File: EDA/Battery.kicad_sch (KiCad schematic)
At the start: 0 parts

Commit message: Changed PD IC from TPS25750DRJKR to TPS25730DREFR
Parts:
- added J1: 12402012E212A, CANSAT-lib:AMPHENOL_USB-C_12402012E212A, symbol CANSAT-lib:12402012E212A
- added U10: TPS25730DREFR, CANSAT-lib:REF0038A-MFG, symbol CANSAT-lib:TPS25730DREFR
- added U9: BQ25895RTWT, CANSAT-lib:QFN50P400X400X80-25N, symbol CANSAT-lib:BQ25895RTWT
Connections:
- new net: U10.11 (GND), U10.12 (GND), U10.14 (GND), U10.16 (GND), U10.17 (GND), U10.31 (GND), U10.34 (GND), U10.35 (GND)
- new net CC1_A: J1.A5 (CC1_A), U10.28 (CC1)
- new net CC1_B: J1.B5 (CC1_B), U10.29 (CC2)
- new net D+: J1.A6 (D+_A), J1.B6 (D+_B)
- new net D-: J1.A7 (D-_A), J1.B7 (D-_B)
- new net GND: J1.A1_B12 (GND), J1.B1_A12 (GND__1), J1.SH1 (SHIELD), J1.SH2 (SHIELD__1), J1.SH3 (SHIELD__2), J1.SH4 (SHIELD__3)
- new net VBUS: J1.A4_B9 (VBUS), J1.B4_A9 (VBUS__1), U10.23 (VBUS_IN), U10.24 (VBUS_IN), U10.25 (VBUS_IN)
- no-connect marks 0 -> 6

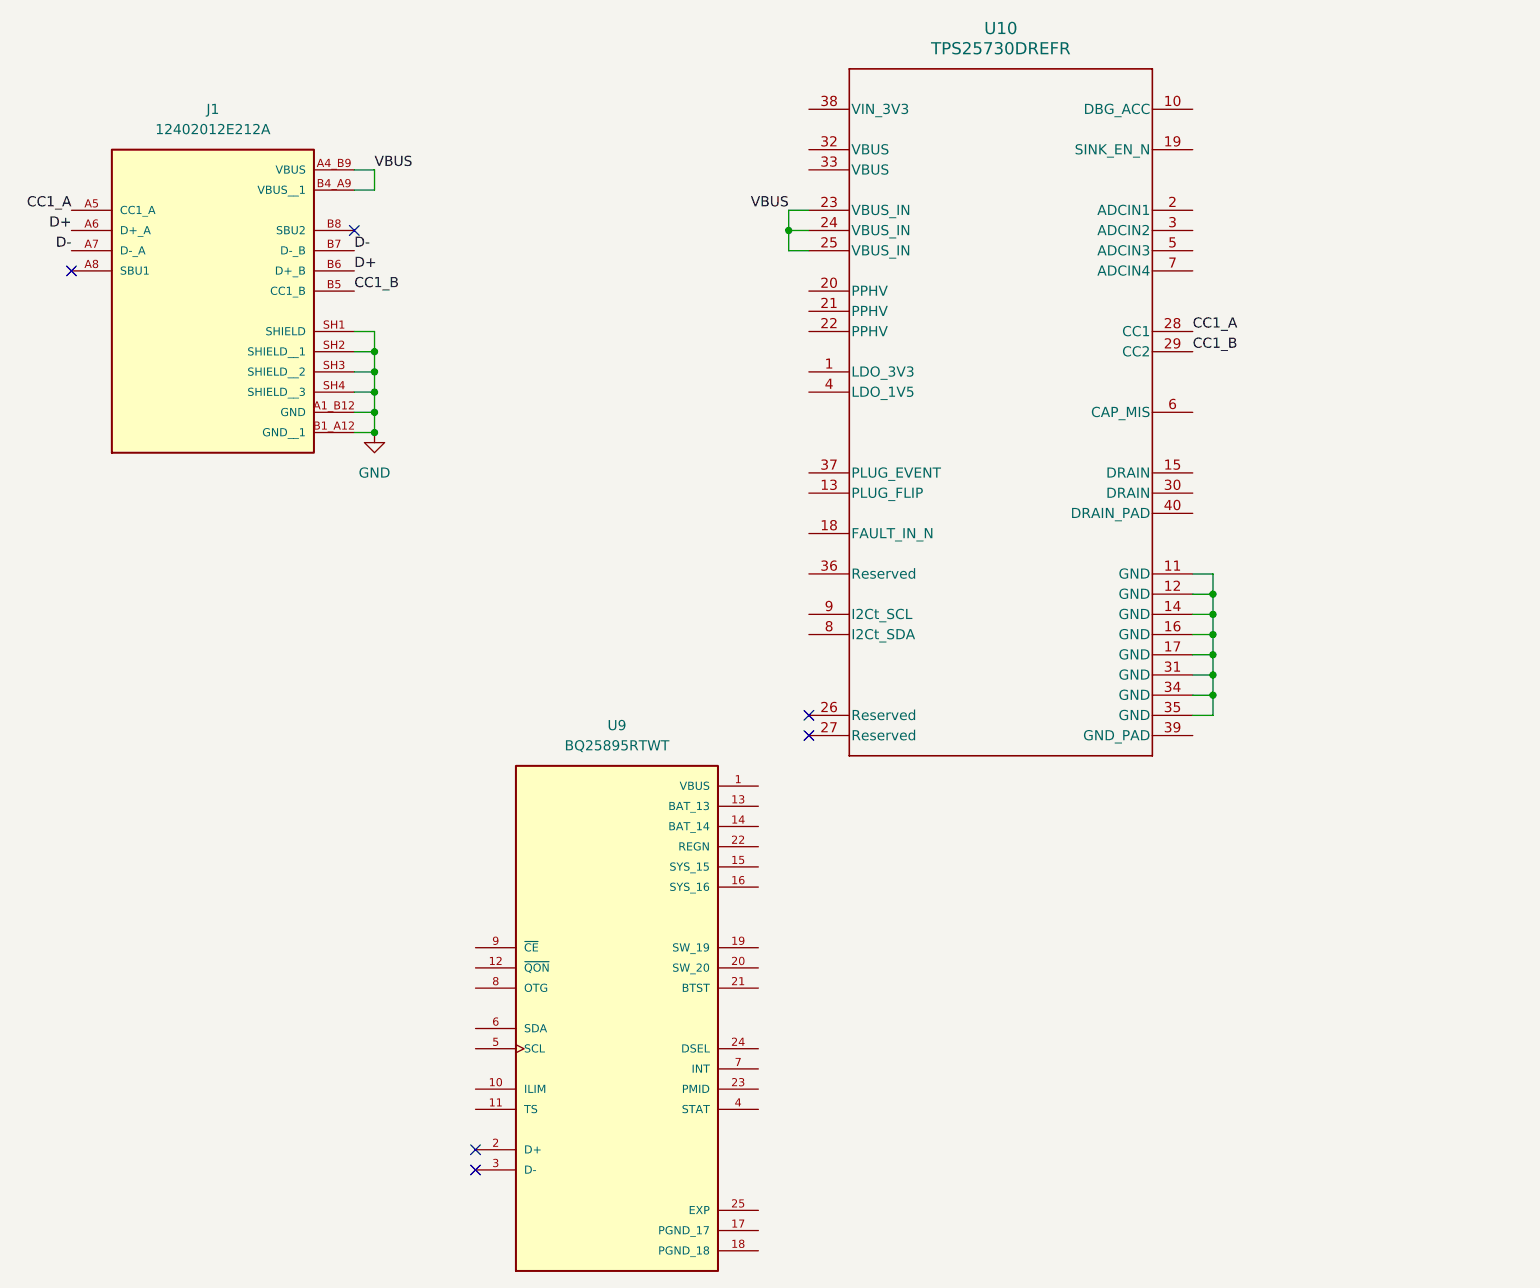
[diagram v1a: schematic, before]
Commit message: added smoothing capacitors to PD IC
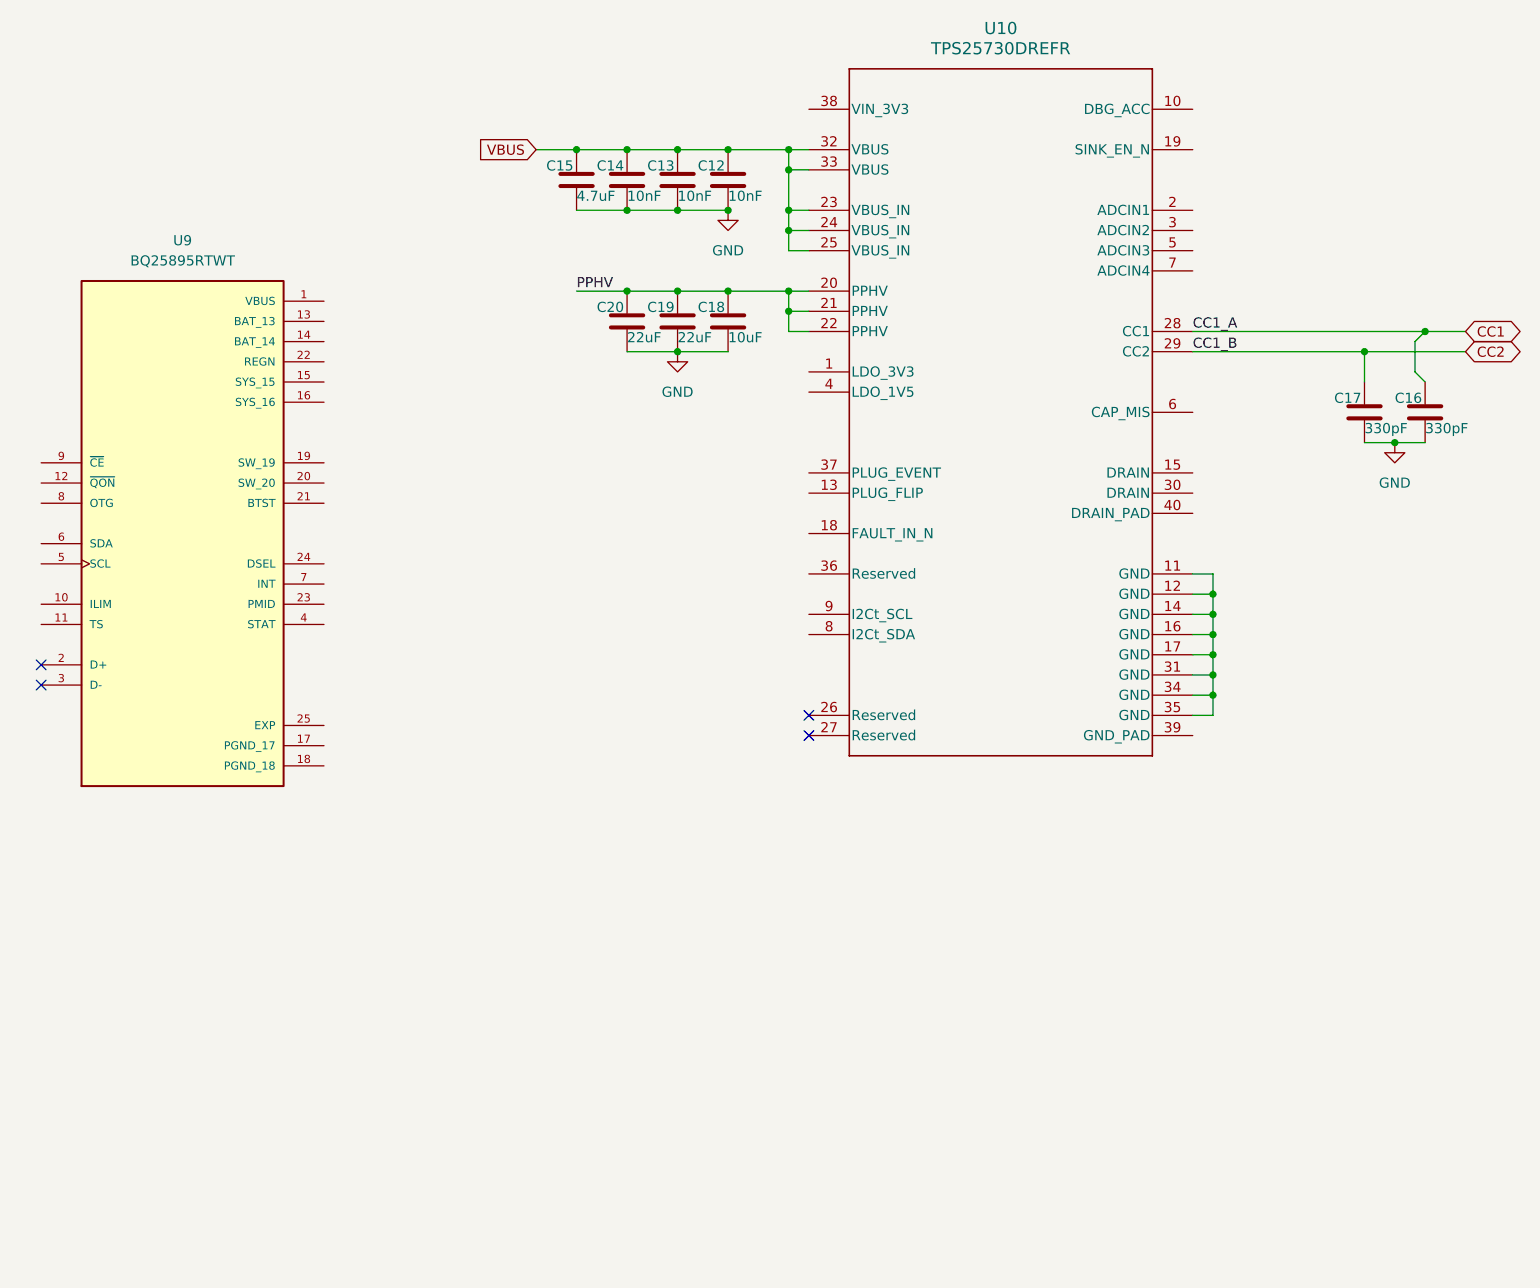
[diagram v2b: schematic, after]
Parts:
- removed J1: 12402012E212A, CANSAT-lib:AMPHENOL_USB-C_12402012E212A, symbol CANSAT-lib:12402012E212A
- added C12, C13, C14: 10nF, symbol Device:C
- added C15: 4.7uF, symbol Device:C
- added C16, C17: 330pF, symbol Device:C
- added C18: 10uF, symbol Device:C
- added C19, C20: 22uF, symbol Device:C
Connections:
- net GND: now also C12.2, C13.2, C14.2, C15.2, C16.2, C17.2, C18.2, C19.2, C20.2
- net VBUS: now also U10.32 (VBUS), U10.33 (VBUS), C12.1, C13.1, C14.1, C15.1
- net PPHV: now reaches U10.20 (PPHV)
- net PPHV: now also U10.21 (PPHV), U10.22 (PPHV), C18.1, C19.1, C20.1
- net CC1_A renamed CC1
- net CC1: now also C16.1
- net CC1_B renamed CC2
- net CC2: now also C17.1
- no-connect marks 6 -> 4
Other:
- moved on the sheet: U9

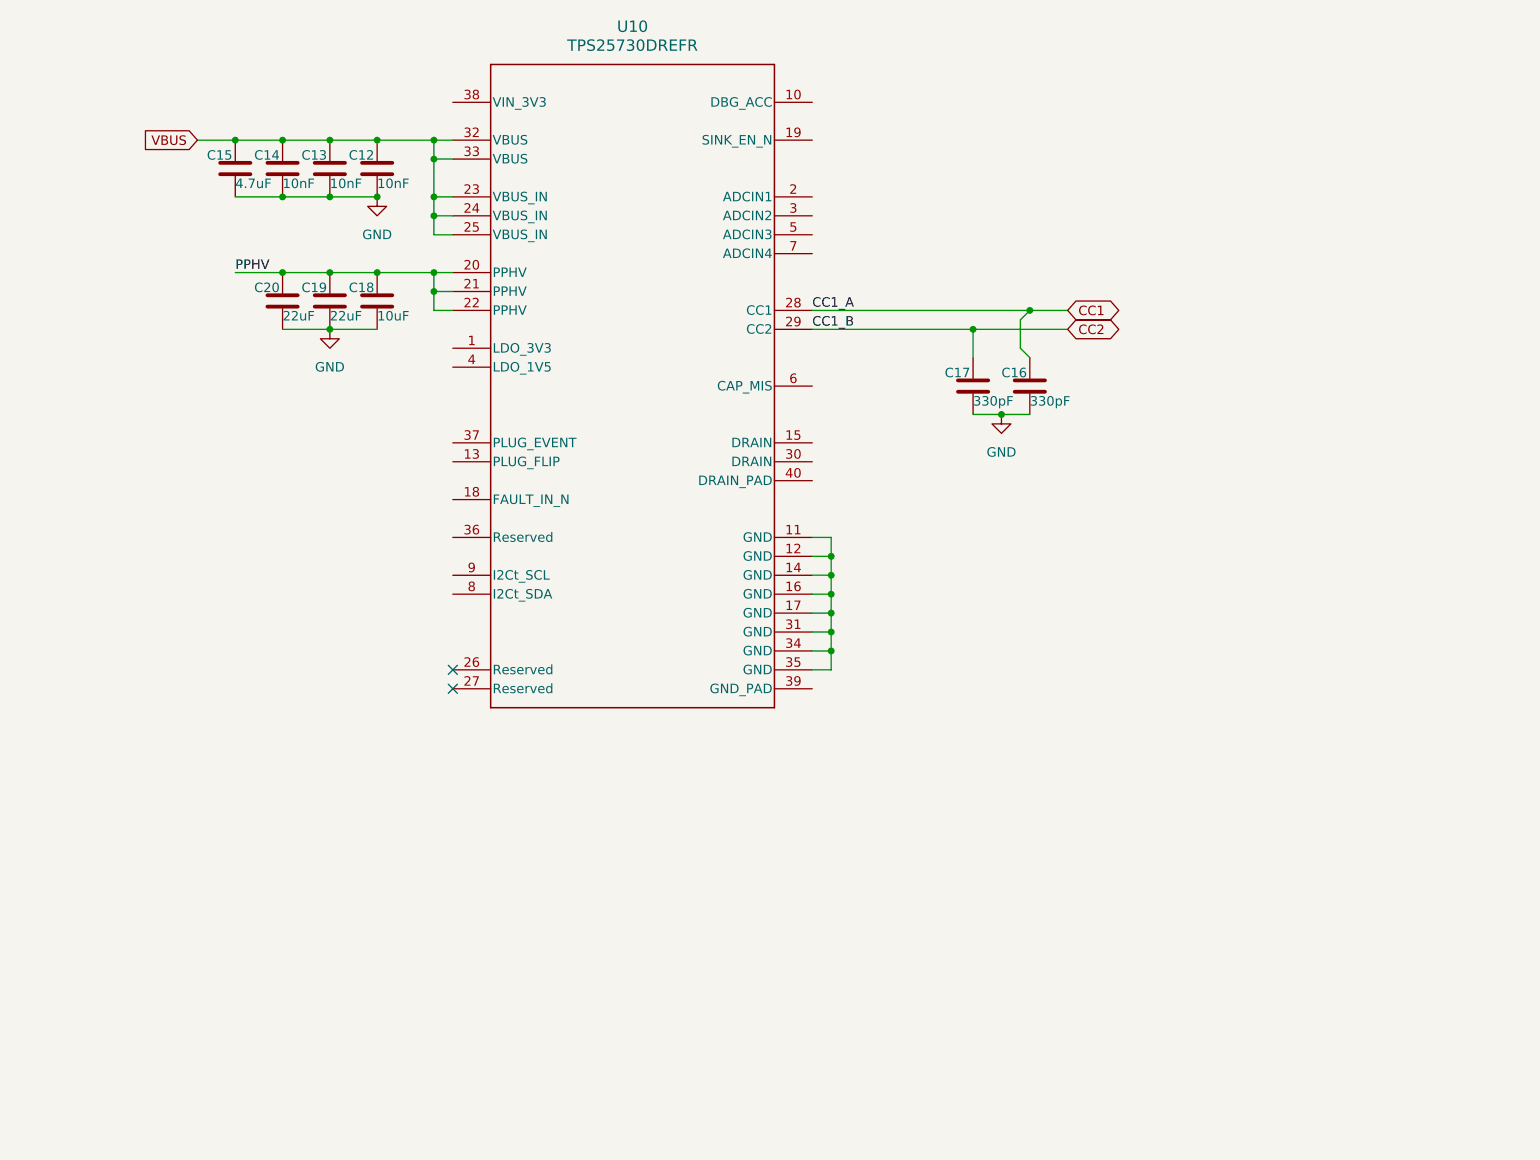
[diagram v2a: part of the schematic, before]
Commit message: PD negotiator IC wired up in schematic
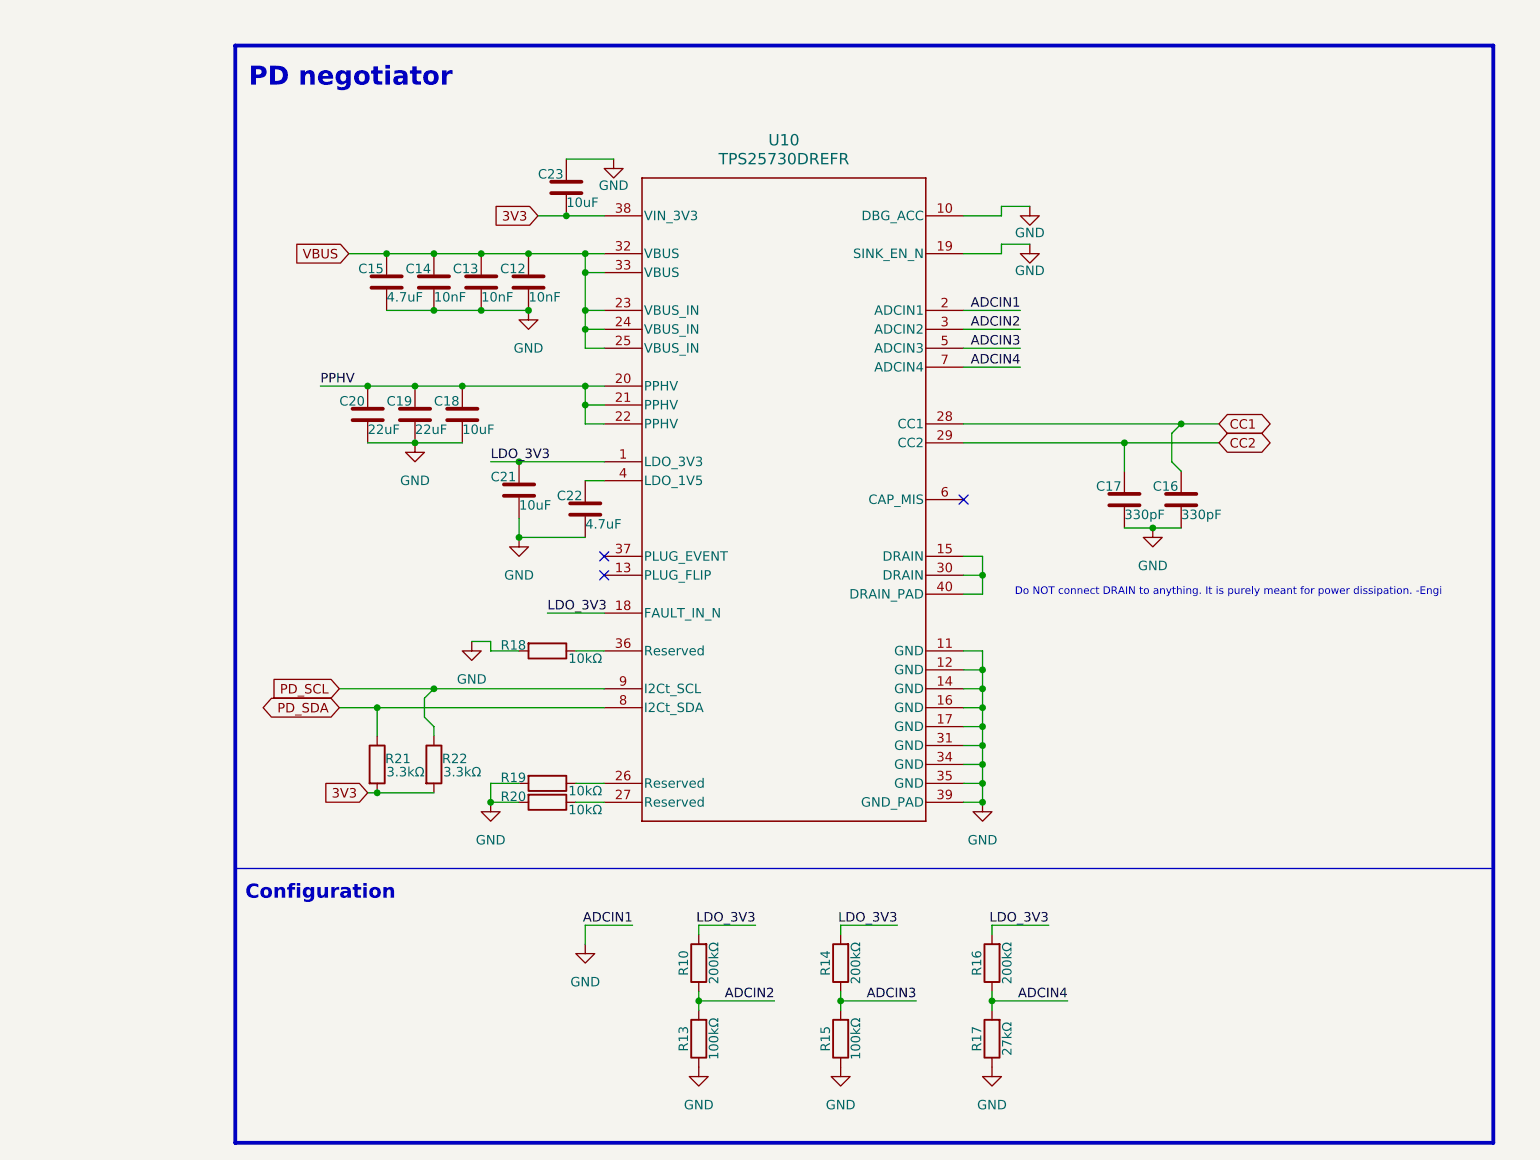
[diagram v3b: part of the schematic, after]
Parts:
- added C21, C23: 10uF, symbol Device:C
- added C22: 4.7uF, symbol Device:C
- added R10, R14, R16: 200kΩ, symbol Device:R
- added R13, R15: 100kΩ, symbol Device:R
- added R17: 27kΩ, symbol Device:R
- added R18, R19, R20: 10kΩ, symbol Device:R
- added R21, R22: 3.3kΩ, symbol Device:R
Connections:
- net GND: now also U10.10 (DBG_ACC), U10.11 (GND), U10.12 (GND), U10.14 (GND), U10.16 (GND), U10.17 (GND), U10.19 (SINK_EN_N), U10.2 (ADCIN1), U10.31 (GND), U10.34 (GND), U10.35 (GND), U10.39 (GND_PAD), C21.2, C22.2, C23.1, R13.1, R15.1, R17.1, R18.2, R19.2, R20.2
- net LDO_3V3: now reaches U10.1 (LDO_3V3)
- net LDO_3V3: now also U10.18 (FAULT_IN_N), C21.1, R10.2, R14.2, R16.2
- net at U10.15 (DRAIN): now also U10.30 (DRAIN), U10.40 (DRAIN_PAD)
- net at U10.26 (Reserved): now also R19.1
- net at U10.27 (Reserved): now also R20.1
- net ADCIN2: now reaches U10.3 (ADCIN2)
- net ADCIN2: now also R10.1, R13.2
- net at U10.36 (Reserved): now also R18.1
- net 3V3: now reaches U10.38 (VIN_3V3)
- net 3V3: now also C23.2, R21.2, R22.2
- net at U10.4 (LDO_1V5): now also C22.1
- net ADCIN3: now reaches U10.5 (ADCIN3)
- net ADCIN3: now also R14.1, R15.2
- net ADCIN4: now reaches U10.7 (ADCIN4)
- net ADCIN4: now also R16.1, R17.2
- net PD_SDA: now reaches U10.8 (I2Ct_SDA)
- net PD_SDA: now also R21.1
- net PD_SCL: now reaches U10.9 (I2Ct_SCL)
- net PD_SCL: now also R22.1
- no-connect marks 4 -> 5
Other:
- note added: "Configuration"
- note added: "Do NOT connect DRAIN to anything. It is purely meant for power dissipation. -Engi"
- note added: "PD negotiator"
- moved on the sheet: C12, C13, C14, C15, C16, C17, C18, C19, C20, U10

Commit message: Did some scheamtic restruscturing as well as hooked up SDRAM and Micro-SD to STM32 core. Additional low power STM32 has also been added to power control. Firmware .IOC files have also been added for both STM32's
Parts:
- added C24, C30: 1uF, symbol Device:C
- added C25, C26: 10pF, symbol Device:C
- added C27, C28: 100nF, symbol Device:C
- added C29: 10uF, symbol Device:C
- added R23, R24, R26: 10kΩ, symbol Device:R
- added R25: 150Ω, symbol Device:R
- added U11: STM32L031G6U6, CANSAT-lib:UFQFPN28-4x4mm, symbol CANSAT-lib:STM32L031G6U6
- added Y1: ABS07-32.768KHZ-T, CANSAT-lib:XTAL_ABS07-32.768KHZ-T, symbol CANSAT-lib:ABS07-32.768KHZ-T
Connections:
- net PD_SCL is gone; now on net PWR_SCL: R22.1, U10.9 (I2Ct_SCL)
- net PD_SDA is gone; now on net PWR_SDA: R21.1, U10.8 (I2Ct_SDA)
- net 3V3: now also R23.2, R24.2, R26.2
- net GND: now also U9.17 (PGND_17), U9.18 (PGND_18), U9.24 (DSEL), U9.25 (EXP), U9.8 (OTG), U9.9 (~{CE}), C24.1, C25.1, C26.1, C27.2, C28.1, C29.1, C30.2, R25.1, U11.16 (VSS), U11.28 (VSS)
- net PPHV: now also U9.1 (VBUS), C24.2
- net BAT_ILIM: now reaches U9.10 (ILIM)
- net BAT_ILIM: now also R25.2
- net BAT_TS: now reaches U9.11 (TS)
- net BAT_STAT: now reaches U9.4 (STAT)
- net PWR_SCL: now reaches U9.5 (SCL)
- net PWR_SCL: now also R23.1, U11.19 (PA9)
- net PWR_SDA: now reaches U9.6 (SDA)
- net PWR_SDA: now also R24.1, U11.20 (PA10)
- net BAT_INT: now reaches U9.7 (INT)
- net BAT_INT: now also R26.1
- new net OSC_IN: C25.2, U11.2 (PC14-OSC32_IN), Y1.2
- new net OSC_OUT: C26.2, U11.3 (PC15-OSC32_OUT), Y1.1
- new net PWR_MCU_3V3: C27.1, C28.2, C29.2, C30.1, U11.1 (VDD), U11.17 (VDD), U11.5 (VDDA)
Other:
- moved on the sheet: C12, C13, C14, C15, C16, C17, C18, C19, C20, C21, C22, C23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
